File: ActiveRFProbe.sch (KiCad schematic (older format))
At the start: 70 parts, among them J1 Conn_01x01, J10 Conn_01x01, J11 Conn_01x01, J12 Conn_01x01, J13 Conn_01x01, J14 Conn_01x01, J15 Conn_01x01, J16 Conn_01x01, J17 Conn_01x01, J18 Conn_01x01, J19 Conn_01x01, J2 Conn_01x01, J20 Conn_01x01, J21 Conn_01x01, J22 Conn_01x01, J23 Conn_01x01, J24 Conn_01x01, J25 Conn_Coaxial, J3 Conn_01x01, J4 Conn_01x01, J5 Conn_01x01, J6 Conn_01x01, J7 Conn_01x01, J8 Conn_01x01, J9 Conn_01x01, Q1 S9018, Q2 S9018, Q3 S9018, Q4 MMBT3904, Q6 MMBT3904, Q7 MMBT3906, SW2 SW_DPDT_x2

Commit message: Fixed envelope detector
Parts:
- added C?: 22 uF, Capacitors_SMD:C_1210_HandSoldering, symbol C_Small
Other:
- moved on the sheet: D5, R9
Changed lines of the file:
@@
 L R R9
 U 1 1 5E9BA4DA
-P 6150 4450
-F 0 "R9" V 6230 4450 50  0000 C CNN
-F 1 "1k" V 6150 4450 50  0000 C CNN
-F 2 "Resistors_SMD:R_0805_HandSoldering" V 6080 4450 50  0001 C CNN
-F 3 "" H 6150 4450 50  0001 C CNN
-	1    6150 4450
+P 6050 4450
+F 0 "R9" V 6130 4450 50  0000 C CNN
+F 1 "1k" V 6050 4450 50  0000 C CNN
+F 2 "Resistors_SMD:R_0805_HandSoldering" V 5980 4450 50  0001 C CNN
+F 3 "" H 6050 4450 50  0001 C CNN
+	1    6050 4450
 	0    1    1    0
 $EndComp
@@
 $EndComp
 $Comp
-L D_Schottky D5
-U 1 1 5E9C8115
-P 6400 4650
-F 0 "D5" H 6400 4750 50  0000 C CNN
-F 1 "LRB751V" H 6400 4550 50  0000 C CNN
-F 2 "Diodes_SMD:D_SOD-323_HandSoldering" H 6400 4650 50  0001 C CNN
-F 3 "" H 6400 4650 50  0001 C CNN
-	1    6400 4650
-	0    1    1    0
-$EndComp
-$Comp
-L GND #PWR08
-U 1 1 5E9C8204
-P 6400 4950
-F 0 "#PWR08" H 6400 4700 50  0001 C CNN
-F 1 "GND" H 6400 4800 50  0000 C CNN
-F 2 "" H 6400 4950 50  0001 C CNN
-F 3 "" H 6400 4950 50  0001 C CNN
-	1    6400 4950
-	1    0    0    -1
-$EndComp
-$Comp
 L SW_DPDT_x2 SW2
 U 2 1 5E9C68E1
@@
 Connection ~ 3800 1250
 Wire Wire Line
-	6400 4950 6400 4800
-Wire Wire Line
 	9650 4700 9650 5000
 Wire Wire Line
@@
 	2900 1350 2900 1250
 Connection ~ 3300 1250
-Wire Wire Line
-	10050 4200 10400 4200
 Wire Wire Line
 	9750 4200 9650 4200
@@
 Connection ~ 5700 4250
 Wire Wire Line
-	5900 4450 6000 4450
-Wire Wire Line
-	6400 4450 6400 4500
-Wire Wire Line
-	6300 4450 6850 4450
+	5900 4450 5900 4450
+Wire Wire Line
+	6600 4450 6850 4450
 $Comp
 L GND #PWR025
@@
 Wire Wire Line
 	6750 4300 6750 4550
-Connection ~ 6400 4450
 Connection ~ 6750 4450
 Wire Wire Line
@@
 Wire Wire Line
 	6600 5500 6600 4450
-Connection ~ 6600 4450
 Text Notes 8400 6950 0    60   ~ 0
 Active RF Probe\nBy D. Marks KW4TI\nCC-BY-SA 4.0
+$Comp
+L D_Schottky D5
+U 1 1 5E9C8115
+P 6450 4450
+F 0 "D5" H 6450 4550 50  0000 C CNN
+F 1 "LRB751V" H 6450 4350 50  0000 C CNN
+F 2 "Diodes_SMD:D_SOD-323_HandSoldering" H 6450 4450 50  0001 C CNN
+F 3 "" H 6450 4450 50  0001 C CNN
+	1    6450 4450
+	-1   0    0    1
+$EndComp
+Wire Wire Line
+	6300 4450 6200 4450
+$Comp
+L C_Small C?
+U 1 1 5E9E2E27
+P 10200 4200
+F 0 "C?" H 10210 4270 50  0000 L CNN
+F 1 "22 uF" H 10210 4120 50  0000 L CNN
+F 2 "Capacitors_SMD:C_1210_HandSoldering" H 10200 4200 50  0001 C CNN
+F 3 "" H 10200 4200 50  0001 C CNN
+	1    10200 4200
+	0    -1   -1   0
+$EndComp
+Wire Wire Line
+	10400 4200 10300 4200
+Wire Wire Line
+	10100 4200 10050 4200
 $EndSCHEMATC

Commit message: Made the board smaller
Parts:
- removed C10, C11: 100 nF, Capacitors_SMD:C_0805_HandSoldering, symbol C_Small
- removed C14: 1 uF, Capacitors_SMD:C_0805_HandSoldering, symbol C_Small
- removed C?: 22 uF, Capacitors_SMD:C_1210_HandSoldering, symbol C_Small
- removed D4: LED, LEDs:LED_0805_HandSoldering, symbol LED
- removed D7, D8: 1N4148WS, Diodes_SMD:D_SOD-323, symbol D
- removed J10, J11, J12, J13, J14, J15, J4, J5, J6, J7, J8, J9: Conn_01x01, ActiveRFProbe:BigSlot, symbol Conn_01x01
- removed Q4, Q6: MMBT3904, TO_SOT_Packages_SMD:SOT-23, symbol MMBT3904
- removed Q7: MMBT3906, TO_SOT_Packages_SMD:SOT-23, symbol MMBT3906
- removed R11, R13: 1k, Resistors_SMD:R_0805_HandSoldering, symbol R
- removed R12, R15, R16: 10k, Resistors_SMD:R_0805_HandSoldering, symbol R
- removed R17: 100R, Resistors_SMD:R_0805_HandSoldering, symbol R
- removed RV1: 100k, Potentiometers:Potentiometer_Triwood_RM-065, symbol POT_TRIM
- removed SW2: SW_DPDT_x2, ActiveRFProbe:DPDTsmallswitch, symbol SW_DPDT_x2
- J1, J16, J17, J18, J19, J24: footprint Connectors:1pin -> ActiveRFProbe:PadHole
- J2, J3: footprint ActiveRFProbe:BigSlot -> ActiveRFProbe:PadHole
- R9: value 1k -> 10k
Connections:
- wire segments 92 -> 61
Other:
- moved on the sheet: C16, D6, J16, J17, J18, J19, J20, J21, J22, J23, J24, R14

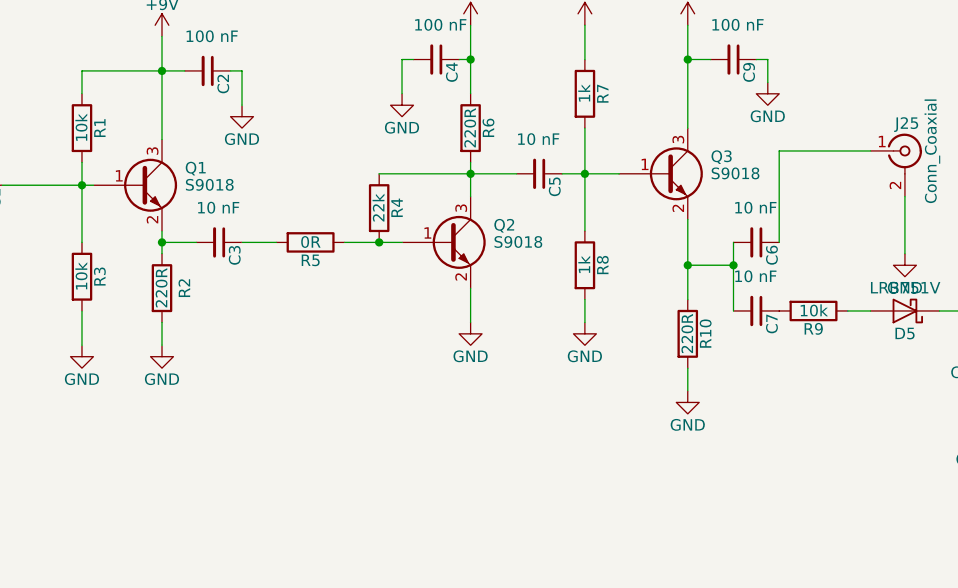
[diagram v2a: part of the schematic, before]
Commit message: Changed transistor to 2SC4083
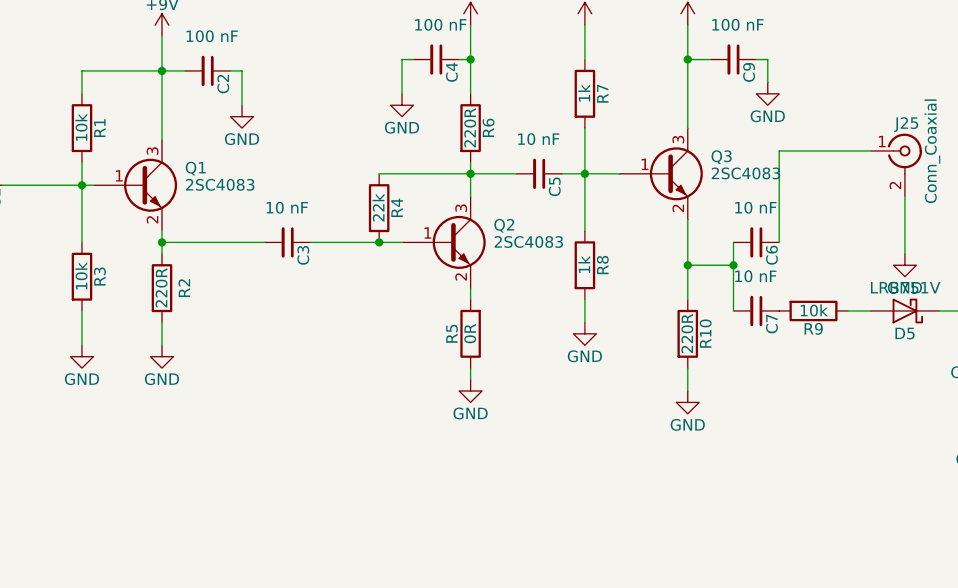
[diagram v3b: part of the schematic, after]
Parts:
- Q1, Q2, Q3: value S9018 -> 2SC4083; footprint TO_SOT_Packages_SMD:SOT-23 -> TO_SOT_Packages_SMD:SOT-323_SC-70_Handsoldering
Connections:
- net GND: now also R5.1; no longer Q2.2 (E)
- net at C3.1: now also Q2.1 (B), R4.2; no longer R5.2
- new net: Q2.2 (E), R5.2
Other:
- moved on the sheet: C3, R5
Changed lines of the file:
@@
 P 3100 3900
 F 0 "Q1" H 3300 3975 50  0000 L CNN
-F 1 "S9018" H 3300 3900 50  0000 L CNN
-F 2 "TO_SOT_Packages_SMD:SOT-23" H 3300 3825 50  0001 L CIN
+F 1 "2SC4083" H 3300 3900 50  0000 L CNN
+F 2 "TO_SOT_Packages_SMD:SOT-323_SC-70_Handsoldering" H 3300 3825 50  0001 L CIN
 F 3 "" H 3100 3900 50  0001 L CNN
 	1    3100 3900
@@
 $EndComp
 $Comp
-L GND #PWR6
+L GND #PWR01
 U 1 1 5E9B90E6
 P 3200 4600
-F 0 "#PWR6" H 3200 4350 50  0001 C CNN
+F 0 "#PWR01" H 3200 4350 50  0001 C CNN
 F 1 "GND" H 3200 4450 50  0000 C CNN
 F 2 "" H 3200 4600 50  0001 C CNN
@@
 L C_Small C3
 U 1 1 5E9B92CF
-P 3450 4150
-F 0 "C3" H 3460 4220 50  0000 L CNN
-F 1 "10 nF" V 3300 4050 50  0000 L CNN
-F 2 "Capacitors_SMD:C_0805_HandSoldering" H 3450 4150 50  0001 C CNN
-F 3 "" H 3450 4150 50  0001 C CNN
-	1    3450 4150
+P 3750 4150
+F 0 "C3" H 3760 4220 50  0000 L CNN
+F 1 "10 nF" V 3600 4050 50  0000 L CNN
+F 2 "Capacitors_SMD:C_0805_HandSoldering" H 3750 4150 50  0001 C CNN
+F 3 "" H 3750 4150 50  0001 C CNN
+	1    3750 4150
 	0    1    1    0
 $EndComp
@@
 P 4450 4150
 F 0 "Q2" H 4650 4225 50  0000 L CNN
-F 1 "S9018" H 4650 4150 50  0000 L CNN
-F 2 "TO_SOT_Packages_SMD:SOT-23" H 4650 4075 50  0001 L CIN
+F 1 "2SC4083" H 4650 4150 50  0000 L CNN
+F 2 "TO_SOT_Packages_SMD:SOT-323_SC-70_Handsoldering" H 4650 4075 50  0001 L CIN
 F 3 "" H 4450 4150 50  0001 L CNN
 	1    4450 4150
@@
 $EndComp
 $Comp
-L GND #PWR13
+L GND #PWR02
 U 1 1 5E9B935A
-P 4550 4500
-F 0 "#PWR13" H 4550 4250 50  0001 C CNN
-F 1 "GND" H 4550 4350 50  0000 C CNN
-F 2 "" H 4550 4500 50  0001 C CNN
-F 3 "" H 4550 4500 50  0001 C CNN
-	1    4550 4500
+P 4550 4750
+F 0 "#PWR02" H 4550 4500 50  0001 C CNN
+F 1 "GND" H 4550 4600 50  0000 C CNN
+F 2 "" H 4550 4750 50  0001 C CNN
+F 3 "" H 4550 4750 50  0001 C CNN
+	1    4550 4750
 	1    0    0    -1
 $EndComp
@@
 L R R5
 U 1 1 5E9B9742
-P 3850 4150
-F 0 "R5" V 3930 4150 50  0000 C CNN
-F 1 "0R" V 3850 4150 50  0000 C CNN
-F 2 "Resistors_SMD:R_0805_HandSoldering" V 3780 4150 50  0001 C CNN
-F 3 "" H 3850 4150 50  0001 C CNN
-	1    3850 4150
-	0    1    1    0
+P 4550 4550
+F 0 "R5" V 4630 4550 50  0000 C CNN
+F 1 "0R" V 4550 4550 50  0000 C CNN
+F 2 "Resistors_SMD:R_0805_HandSoldering" V 4480 4550 50  0001 C CNN
+F 3 "" H 4550 4550 50  0001 C CNN
+	1    4550 4550
+	-1   0    0    1
 $EndComp
 $Comp
@@
 P 5400 3850
 F 0 "Q3" H 5600 3925 50  0000 L CNN
-F 1 "S9018" H 5600 3850 50  0000 L CNN
-F 2 "TO_SOT_Packages_SMD:SOT-23" H 5600 3775 50  0001 L CIN
+F 1 "2SC4083" H 5600 3850 50  0000 L CNN
+F 2 "TO_SOT_Packages_SMD:SOT-323_SC-70_Handsoldering" H 5600 3775 50  0001 L CIN
 F 3 "" H 5400 3850 50  0001 L CNN
 	1    5400 3850
@@
 $EndComp
 $Comp
-L GND #PWR2
+L GND #PWR03
 U 1 1 5E9BF682
 P 2100 4500
-F 0 "#PWR2" H 2100 4250 50  0001 C CNN
+F 0 "#PWR03" H 2100 4250 50  0001 C CNN
 F 1 "GND" H 2100 4350 50  0000 C CNN
 F 2 "" H 2100 4500 50  0001 C CNN
@@
 $EndComp
 $Comp
-L GND #PWR9
+L GND #PWR04
 U 1 1 5E9C1122
 P 3100 2550
-F 0 "#PWR9" H 3100 2300 50  0001 C CNN
+F 0 "#PWR04" H 3100 2300 50  0001 C CNN
 F 1 "GND" H 3100 2400 50  0000 C CNN
 F 2 "" H 3100 2550 50  0001 C CNN
@@
 $EndComp
 $Comp
-L GND #PWR1
+L GND #PWR05
 U 1 1 5E9C57D4
 P 1950 3500
-F 0 "#PWR1" H 1950 3250 50  0001 C CNN
+F 0 "#PWR05" H 1950 3250 50  0001 C CNN
 F 1 "GND" H 1950 3350 50  0000 C CNN
 F 2 "" H 1950 3500 50  0001 C CNN
@@
 $EndComp
 $Comp
-L +9V #PWR8
+L +9V #PWR06
 U 1 1 5E9C9102
 P 3100 1500
-F 0 "#PWR8" H 3100 1350 50  0001 C CNN
+F 0 "#PWR06" H 3100 1350 50  0001 C CNN
 F 1 "+9V" H 3100 1640 50  0000 C CNN
 F 2 "" H 3100 1500 50  0001 C CNN
@@
 $EndComp
 $Comp
-L GND #PWR4
+L GND #PWR07
 U 1 1 5E9CFF23
 P 2200 2500
-F 0 "#PWR4" H 2200 2250 50  0001 C CNN
+F 0 "#PWR07" H 2200 2250 50  0001 C CNN
 F 1 "GND" H 2200 2350 50  0000 C CNN
 F 2 "" H 2200 2500 50  0001 C CNN
@@
 $EndComp
 $Comp
-L GND #PWR3
+L GND #PWR08
 U 1 1 5E9D5800
 P 2850 4600
-F 0 "#PWR3" H 2850 4350 50  0001 C CNN
+F 0 "#PWR08" H 2850 4350 50  0001 C CNN
 F 1 "GND" H 2850 4450 50  0000 C CNN
 F 2 "" H 2850 4600 50  0001 C CNN
@@
 $EndComp
 $Comp
-L +9V #PWR5
+L +9V #PWR09
 U 1 1 5E9D5F5F
 P 3200 3250
-F 0 "#PWR5" H 3200 3100 50  0001 C CNN
+F 0 "#PWR09" H 3200 3100 50  0001 C CNN
 F 1 "+9V" H 3200 3390 50  0000 C CNN
 F 2 "" H 3200 3250 50  0001 C CNN
@@
 $EndComp
 $Comp
-L GND #PWR7
+L GND #PWR010
 U 1 1 5E9D6577
 P 3550 3550
-F 0 "#PWR7" H 3550 3300 50  0001 C CNN
+F 0 "#PWR010" H 3550 3300 50  0001 C CNN
 F 1 "GND" H 3550 3400 50  0000 C CNN
 F 2 "" H 3550 3550 50  0001 C CNN
@@
 $EndComp
 $Comp
-L +9V #PWR12
+L +9V #PWR011
 U 1 1 5E9D7A25
 P 4550 3200
-F 0 "#PWR12" H 4550 3050 50  0001 C CNN
+F 0 "#PWR011" H 4550 3050 50  0001 C CNN
 F 1 "+9V" H 4550 3340 50  0000 C CNN
 F 2 "" H 4550 3200 50  0001 C CNN
@@
 $EndComp
 $Comp
-L GND #PWR11
+L GND #PWR012
 U 1 1 5E9D80F3
 P 4250 3500
-F 0 "#PWR11" H 4250 3250 50  0001 C CNN
+F 0 "#PWR012" H 4250 3250 50  0001 C CNN
 F 1 "GND" H 4250 3350 50  0000 C CNN
 F 2 "" H 4250 3500 50  0001 C CNN
@@
 $EndComp
 $Comp
-L GND #PWR15
+L GND #PWR013
 U 1 1 5E9D893B
 P 5050 4500
-F 0 "#PWR15" H 5050 4250 50  0001 C CNN
+F 0 "#PWR013" H 5050 4250 50  0001 C CNN
 F 1 "GND" H 5050 4350 50  0000 C CNN
 F 2 "" H 5050 4500 50  0001 C CNN
@@
 $EndComp
 $Comp
-L +9V #PWR14
+L +9V #PWR014
 U 1 1 5E9D8F00
 P 5050 3200
-F 0 "#PWR14" H 5050 3050 50  0001 C CNN
+F 0 "#PWR014" H 5050 3050 50  0001 C CNN
 F 1 "+9V" H 5050 3340 50  0000 C CNN
 F 2 "" H 5050 3200 50  0001 C CNN
@@
 $EndComp
 $Comp
-L GND #PWR17
+L GND #PWR015
 U 1 1 5E9D96E5
 P 5500 4800
-F 0 "#PWR17" H 5500 4550 50  0001 C CNN
+F 0 "#PWR015" H 5500 4550 50  0001 C CNN
 F 1 "GND" H 5500 4650 50  0000 C CNN
 F 2 "" H 5500 4800 50  0001 C CNN
@@
 $EndComp
 $Comp
-L +9V #PWR16
+L +9V #PWR016
 U 1 1 5E9DA181
 P 5500 3200
-F 0 "#PWR16" H 5500 3050 50  0001 C CNN
+F 0 "#PWR016" H 5500 3050 50  0001 C CNN
 F 1 "+9V" H 5500 3340 50  0000 C CNN
 F 2 "" H 5500 3200 50  0001 C CNN
@@
 $EndComp
 $Comp
-L GND #PWR18
+L GND #PWR017
 U 1 1 5E9DA538
 P 5850 3450
-F 0 "#PWR18" H 5850 3200 50  0001 C CNN
+F 0 "#PWR017" H 5850 3200 50  0001 C CNN
 F 1 "GND" H 5850 3300 50  0000 C CNN
 F 2 "" H 5850 3450 50  0001 C CNN
@@
 $EndComp
 $Comp
-L GND #PWR20
+L GND #PWR018
 U 1 1 5E9DC195
 P 6750 4950
-F 0 "#PWR20" H 6750 4700 50  0001 C CNN
+F 0 "#PWR018" H 6750 4700 50  0001 C CNN
 F 1 "GND" H 6750 4800 50  0000 C CNN
 F 2 "" H 6750 4950 50  0001 C CNN
@@
 $EndComp
 $Comp
-L GND #PWR19
+L GND #PWR019
 U 1 1 5E9DE267
 P 6450 4200
-F 0 "#PWR19" H 6450 3950 50  0001 C CNN
+F 0 "#PWR019" H 6450 3950 50  0001 C CNN
 F 1 "GND" H 6450 4050 50  0000 C CNN
 F 2 "" H 6450 4200 50  0001 C CNN
@@
 $EndComp
 $Comp
-L GND #PWR10
+L GND #PWR020
 U 1 1 5E9DEDB9
 P 3500 1900
-F 0 "#PWR10" H 3500 1650 50  0001 C CNN
+F 0 "#PWR020" H 3500 1650 50  0001 C CNN
 F 1 "GND" H 3500 1750 50  0000 C CNN
 F 2 "" H 3500 1900 50  0001 C CNN
@@
 $EndComp
 $Comp
-L GND #PWR21
+L GND #PWR021
 U 1 1 5E9E423A
 P 7150 4950
-F 0 "#PWR21" H 7150 4700 50  0001 C CNN
+F 0 "#PWR021" H 7150 4700 50  0001 C CNN
 F 1 "GND" H 7150 4800 50  0000 C CNN
 F 2 "" H 7150 4950 50  0001 C CNN
@@
 	3200 3250 3200 3700
 Wire Wire Line
-	4550 4500 4550 4350
-Wire Wire Line
 	1950 4000 1950 3900
 Connection ~ 1950 3900
@@
 	2850 4600 2850 4450
 Wire Wire Line
-	3350 4150 3200 4150
+	3650 4150 3200 4150
 Connection ~ 3200 4150
 Wire Wire Line
@@
 	3550 3400 3500 3400
 Wire Wire Line
-	4000 4150 4250 4150
+	3850 4150 4250 4150
 Wire Wire Line
 	4550 3800 4550 3950
@@
 Connection ~ 4550 3850
 Connection ~ 4150 4150
-Wire Wire Line
-	3700 4150 3550 4150
 Wire Wire Line
 	4550 3200 4550 3500
@@
 Wire Wire Line
 	3100 1800 3100 1550
+Wire Wire Line
+	4550 4700 4550 4750
+Wire Wire Line
+	4550 4400 4550 4350
 $EndSCHEMATC

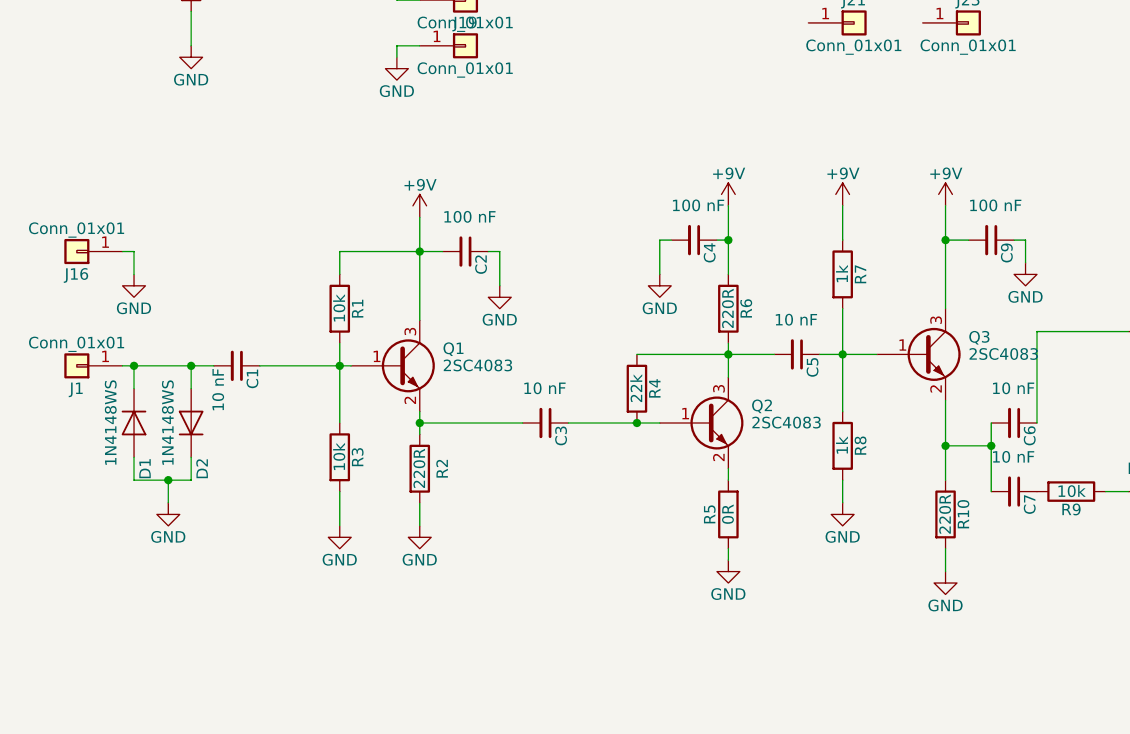
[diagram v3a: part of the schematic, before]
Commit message: Version with SOT-232 2SC4083
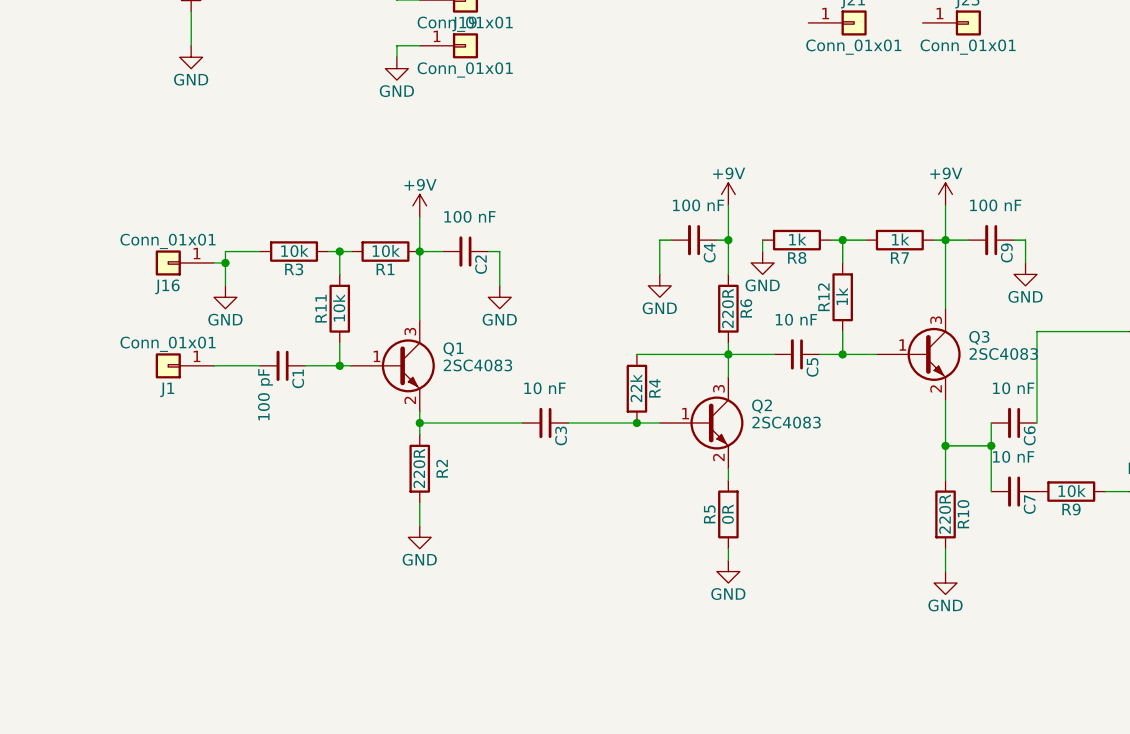
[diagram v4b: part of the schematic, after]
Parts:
- removed D1, D2: 1N4148WS, Diodes_SMD:D_SOD-323_HandSoldering, symbol D
- added R11: 10k, Resistors_SMD:R_0805_HandSoldering, symbol R
- added R12: 1k, Resistors_SMD:R_0805_HandSoldering, symbol R
- C1: value 10 nF -> 100 pF
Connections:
- net at C1.1, Q1.1 (B): now also R11.1; no longer R1.2, R3.1
- net at R7.2, R8.1: now also R12.2; no longer C5.1, Q3.1 (B)
- new net: R1.2, R11.2, R3.1
- new net: C5.1, Q3.1 (B), R12.1
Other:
- moved on the sheet: C1, J1, J16, R1, R3, R7, R8

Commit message: Changed transistor to 2SC3357
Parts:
- removed Q1, Q2, Q3: 2SC4083, TO_SOT_Packages_SMD:SOT-323_SC-70_Handsoldering, symbol MMBT3904
- added Q1, Q2, Q3: 2SC3357, TO_SOT_Packages_SMD:SOT-89-3_Handsoldering, symbol 2SA1015
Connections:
- net +9V: now also Q1.2 (C), Q3.2 (C)
- net at C1.1, R11.1: now also Q1.3 (B)
- net at C3.2, R2.1: now also Q1.1 (E)
- net at C3.1, R4.2: now also Q2.3 (B)
- net at R5.2: now also Q2.1 (E)
- net at C5.2, R4.1, R6.2: now also Q2.2 (C)
- net at C5.1, R12.1: now also Q3.3 (B)
- net at C6.2, C7.2, R10.1: now also Q3.1 (E)
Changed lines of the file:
@@
 $EndDescr
-$Comp
-L MMBT3904 Q1
-U 1 1 5E9B8F33
-P 3100 3900
-F 0 "Q1" H 3300 3975 50  0000 L CNN
-F 1 "2SC4083" H 3300 3900 50  0000 L CNN
-F 2 "TO_SOT_Packages_SMD:SOT-323_SC-70_Handsoldering" H 3300 3825 50  0001 L CIN
-F 3 "" H 3100 3900 50  0001 L CNN
-	1    3100 3900
-	1    0    0    -1
-$EndComp
 $Comp
 L R R1
@@
 $EndComp
 $Comp
-L MMBT3904 Q2
-U 1 1 5E9B9325
-P 4450 4150
-F 0 "Q2" H 4650 4225 50  0000 L CNN
-F 1 "2SC4083" H 4650 4150 50  0000 L CNN
-F 2 "TO_SOT_Packages_SMD:SOT-323_SC-70_Handsoldering" H 4650 4075 50  0001 L CIN
-F 3 "" H 4450 4150 50  0001 L CNN
-	1    4450 4150
-	1    0    0    -1
-$EndComp
-$Comp
 L GND #PWR11
 U 1 1 5E9B935A
@@
 	1    4850 3850
 	0    1    1    0
-$EndComp
-$Comp
-L MMBT3904 Q3
-U 1 1 5E9B9C39
-P 5400 3850
-F 0 "Q3" H 5600 3925 50  0000 L CNN
-F 1 "2SC4083" H 5600 3850 50  0000 L CNN
-F 2 "TO_SOT_Packages_SMD:SOT-323_SC-70_Handsoldering" H 5600 3775 50  0001 L CIN
-F 3 "" H 5400 3850 50  0001 L CNN
-	1    5400 3850
-	1    0    0    -1
 $EndComp
 $Comp
@@
 Wire Wire Line
 	5050 3450 5050 3350
+$Comp
+L 2SA1015 Q1
+U 1 1 5E9DADBE
+P 3100 3900
+F 0 "Q1" H 3300 3975 50  0000 L CNN
+F 1 "2SC3357" H 3300 3900 50  0000 L CNN
+F 2 "TO_SOT_Packages_SMD:SOT-89-3_Handsoldering" H 3300 3825 50  0001 L CIN
+F 3 "" H 3100 3900 50  0001 L CNN
+	1    3100 3900
+	1    0    0    -1
+$EndComp
+$Comp
+L 2SA1015 Q2
+U 1 1 5E9DB0CD
+P 4450 4150
+F 0 "Q2" H 4650 4225 50  0000 L CNN
+F 1 "2SC3357" H 4650 4150 50  0000 L CNN
+F 2 "TO_SOT_Packages_SMD:SOT-89-3_Handsoldering" H 4650 4075 50  0001 L CIN
+F 3 "" H 4450 4150 50  0001 L CNN
+	1    4450 4150
+	1    0    0    -1
+$EndComp
+$Comp
+L 2SA1015 Q3
+U 1 1 5E9DB203
+P 5400 3850
+F 0 "Q3" H 5600 3925 50  0000 L CNN
+F 1 "2SC3357" H 5600 3850 50  0000 L CNN
+F 2 "TO_SOT_Packages_SMD:SOT-89-3_Handsoldering" H 5600 3775 50  0001 L CIN
+F 3 "" H 5400 3850 50  0001 L CNN
+	1    5400 3850
+	1    0    0    -1
+$EndComp
 $EndSCHEMATC
